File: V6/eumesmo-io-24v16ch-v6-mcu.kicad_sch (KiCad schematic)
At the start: 21 parts, among them Q3 UMH3N, SW1 RESET, U3 TPS3820-33, U4 CH340K, U5 ESP32-WROOM-32UE-N16

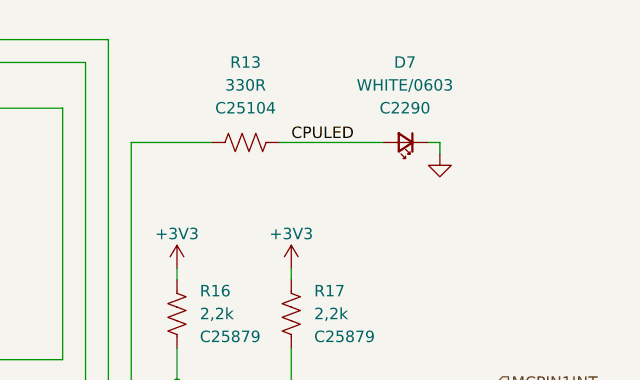
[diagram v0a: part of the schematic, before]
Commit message: Replaced white leds for emerald.
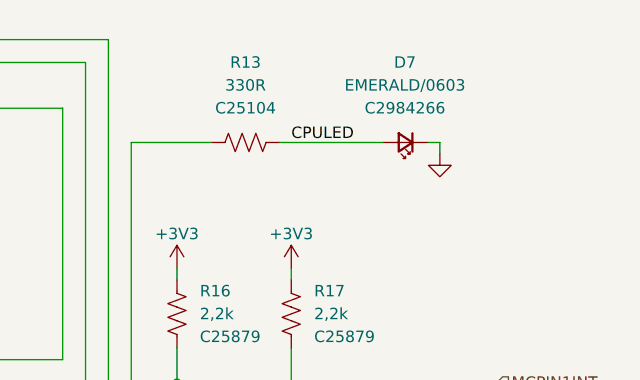
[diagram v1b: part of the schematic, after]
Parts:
- D7: value WHITE/0603 -> EMERALD/0603; LCSC Part # C2290 -> C2984266; Mfr Hubei KENTO Elec -> Everlight Elec; Mfr PN KT-0603W -> 19-213/GHC-XS1T1N/5T; Vendor PN C2290 -> C2984266
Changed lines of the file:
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@@
 			)
 		)
-		(property "Value" "WHITE/0603"
+		(property "Value" "EMERALD/0603"
 			(at 257.7465 35.56 0)
 			(show_name no)
@@
 			)
 		)
-		(property "Mfr" "Hubei KENTO Elec"
+		(property "Mfr" "Everlight Elec"
 			(at 257.81 41.91 0)
 			(hide yes)
@@
 			)
 		)
-		(property "Mfr PN" "KT-0603W"
+		(property "Mfr PN" "19-213/GHC-XS1T1N/5T"
 			(at 257.81 41.91 0)
 			(hide yes)
@@
 			)
 		)
-		(property "Vendor PN" "C2290"
+		(property "Vendor PN" "C2984266"
 			(at 257.81 41.91 0)
 			(hide yes)
@@
 			)
 		)
-		(property "LCSC Part #" "C2290"
+		(property "LCSC Part #" "C2984266"
 			(at 257.7465 38.1 0)
 			(show_name no)

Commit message: Remove jumpers from BOM.
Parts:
- D7: FT Rotation Offset 0 -> 180
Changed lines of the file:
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@@
 			)
 		)
-		(property "FT Rotation Offset" "0"
+		(property "FT Rotation Offset" "180"
 			(at 257.81 41.91 0)
 			(hide yes)

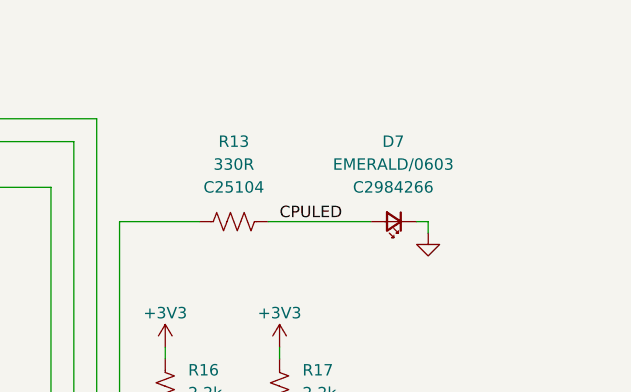
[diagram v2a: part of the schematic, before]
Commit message: LEDs changed to orange
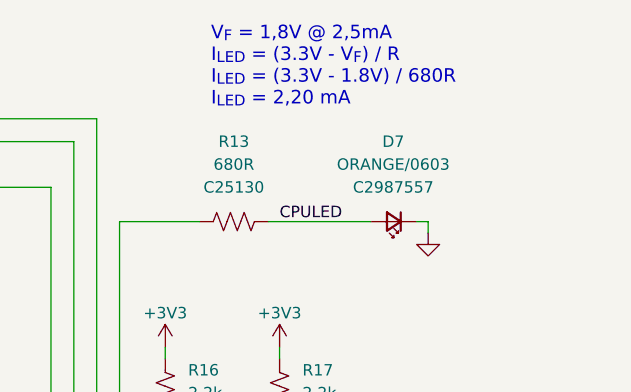
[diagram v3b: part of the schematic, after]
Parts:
- D7: value EMERALD/0603 -> ORANGE/0603; FT Rotation Offset 180 -> 0; LCSC Part # C2984266 -> C2987557; Mfr PN 19-213/GHC-XS1T1N/5T -> 19-217/S2C-AL1M2VY/6T; Vendor PN C2984266 -> C2987557
- R13: value 330R -> 680R; LCSC Part # C25104 -> C25130; Mfr PN 0402WGF3300TCE -> 0402WGF6800TCE; Vendor PN C25104 -> C25130
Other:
- note added: "V_{F} = 1,8V @ 2,5mA I_{LED} = (3.3V - V_{F}) / R I_{LED} = (3.3V - 1.8V) / 680R I_{LED} = 2,20 mA"
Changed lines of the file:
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@@
 		)
 	)
+	(text "V_{F} = 1,8V @ 2,5mA\nI_{LED} = (3.3V - V_{F}) / R\nI_{LED} = (3.3V - 1.8V) / 680R\nI_{LED} = 2,20 mA"
+		(exclude_from_sim no)
+		(at 237.49 29.21 0)
+		(effects
+			(font
+				(size 1.5 1.5)
+			)
+			(justify left bottom)
+		)
+	)
 	(text_box "ESP32 GPIO ASSIGNMENT\n\nPIN	PORT	FUNCTION		COMPONENT\n\n25	GPIO0	AUTO FLASH MODE	0\n35	GPIO1	SERIAL TX		3200\n24	GPIO2	-				0\n34	GPIO3	SERIAL RX		3232\n26	GPIO4	-				0\n29	GPIO5	-				0\n17	GPIO9	-				0\n18	GPIO10	-				0\n14	GPIO12	ETH POWER		5536\n16	GPIO13	MCP23017 INT1	10240\n13	GPIO14	MCP23017 INT2	10241\n23	GPIO15	-				0\n27	GPIO16	DS18X20			1312\n28	GPIO17	ETH CLK			0\n30	GPIO18	ETH MDIO		5600\n31	GPIO19	ETH TXD0		0\n-	GPIO20	-				0\n33	GPIO21	ETH TXEN		0\n36	GPIO22	ETH TXD1		0\n37	GPIO23	ETH MDC			5568\n-	GPIO24	-				0\n10	GPIO25	ETH RXD0		0\n11	GPIO26	ETH RXD1		0\n12	GPIO27	ETH RX			0\n20	GPIO6	-				0\n21	GPIO7	-				0\n22	GPIO8	-				0\n19	GPIO11	-				0\n8	GPIO32	I2C SCL			608\n9	GPIO33	I2C SDA			640\n6	GPIO34	-				0\n7	GPIO35	-				0\n4	GPIO36	-				0\n-	GPIO37	-				0\n-	GPIO38	-				0\n5	GPIO39	-				0"
 		(exclude_from_sim no)
@@
 			)
 		)
-		(property "Value" "EMERALD/0603"
+		(property "Value" "ORANGE/0603"
 			(at 257.7465 35.56 0)
 			(show_name no)
@@
 			)
 		)
-		(property "Mfr PN" "19-213/GHC-XS1T1N/5T"
+		(property "Mfr PN" "19-217/S2C-AL1M2VY/6T"
 			(at 257.81 41.91 0)
 			(hide yes)
@@
 			)
 		)
-		(property "Vendor PN" "C2984266"
+		(property "Vendor PN" "C2987557"
 			(at 257.81 41.91 0)
 			(hide yes)
@@
 			)
 		)
-		(property "LCSC Part #" "C2984266"
+		(property "LCSC Part #" "C2987557"
 			(at 257.7465 38.1 0)
 			(show_name no)
@@
 			)
 		)
-		(property "FT Rotation Offset" "180"
+		(property "FT Rotation Offset" "0"
 			(at 257.81 41.91 0)
 			(hide yes)
@@
 			)
 		)
-		(property "Value" "330R"
+		(property "Value" "680R"
 			(at 240.03 35.56 90)
 			(show_name no)
@@
 			)
 		)
-		(property "Mfr PN" "0402WGF3300TCE"
+		(property "Mfr PN" "0402WGF6800TCE"
 			(at 240.03 41.91 0)
 			(hide yes)
@@
 			)
 		)
-		(property "Vendor PN" "C25104"
+		(property "Vendor PN" "C25130"
 			(at 240.03 41.91 0)
 			(hide yes)
@@
 			)
 		)
-		(property "LCSC Part #" "C25104"
+		(property "LCSC Part #" "C25130"
 			(at 240.03 38.1 90)
 			(show_name no)

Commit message: Adjusted component rotation and offset information for JLCPCB.
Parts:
- U5: FT Position Offset (none) -> 0,-0.65
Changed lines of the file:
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@@
 			)
 		)
+		(property "FT Position Offset" ""
+			(at 257.81 41.91 0)
+			(hide yes)
+			(show_name no)
+			(do_not_autoplace no)
+			(effects
+				(font
+					(size 1.27 1.27)
+				)
+			)
+		)
 		(pin "1"
 		)
@@
 			)
 		)
+		(property "FT Position Offset" ""
+			(at 39.37 67.31 0)
+			(hide yes)
+			(show_name no)
+			(do_not_autoplace no)
+			(effects
+				(font
+					(size 1.27 1.27)
+				)
+			)
+		)
 		(pin "1"
 		)
@@
 			)
 		)
+		(property "FT Position Offset" ""
+			(at 215.9 93.98 90)
+			(hide yes)
+			(show_name no)
+			(do_not_autoplace no)
+			(effects
+				(font
+					(size 1.27 1.27)
+				)
+			)
+		)
 		(pin "2"
 		)
@@
 			)
 		)
-		(property "Package" ""
+		(property "Case" "0805/2012"
 			(at 160.02 53.34 0)
 			(hide yes)
@@
 			)
 		)
-		(property "Case" "0805/2012"
+		(property "FT Rotation Offset" "0"
 			(at 160.02 53.34 0)
 			(hide yes)
@@
 			)
 		)
-		(property "FT Rotation Offset" "0"
+		(property "FT Position Offset" ""
 			(at 160.02 53.34 0)
 			(hide yes)
@@
 			)
 		)
-		(property "Package" ""
+		(property "Case" "0402/1005"
 			(at 123.19 55.88 0)
 			(hide yes)
@@
 			)
 		)
-		(property "Case" "0402/1005"
+		(property "FT Rotation Offset" "0"
 			(at 123.19 55.88 0)
 			(hide yes)
@@
 			)
 		)
-		(property "FT Rotation Offset" "0"
+		(property "FT Position Offset" ""
 			(at 123.19 55.88 0)
 			(hide yes)
@@
 			)
 		)
-		(property "Package" ""
+		(property "Case" "0402/1005"
 			(at 209.55 58.42 0)
 			(hide yes)
@@
 			)
 		)
-		(property "Case" "0402/1005"
+		(property "FT Rotation Offset" "0"
 			(at 209.55 58.42 0)
 			(hide yes)
@@
 			)
 		)
-		(property "FT Rotation Offset" "0"
+		(property "FT Position Offset" ""
 			(at 209.55 58.42 0)
 			(hide yes)
@@
 			)
 		)
+		(property "FT Position Offset" ""
+			(at 182.88 53.34 0)
+			(hide yes)
+			(show_name no)
+			(do_not_autoplace no)
+			(effects
+				(font
+					(size 1.27 1.27)
+				)
+			)
+		)
 		(pin "1"
 		)
@@
 			)
 		)
+		(property "FT Position Offset" ""
+			(at 48.26 67.31 0)
+			(hide yes)
+			(show_name no)
+			(do_not_autoplace no)
+			(effects
+				(font
+					(size 1.27 1.27)
+				)
+			)
+		)
 		(pin "1"
 		)
@@
 			)
 		)
+		(property "FT Position Offset" ""
+			(at 106.68 59.69 0)
+			(hide yes)
+			(show_name no)
+			(do_not_autoplace no)
+			(effects
+				(font
+					(size 1.27 1.27)
+				)
+			)
+		)
 		(pin "1"
 		)
@@
 			)
 		)
+		(property "FT Position Offset" ""
+			(at 106.68 80.01 0)
+			(hide yes)
+			(show_name no)
+			(do_not_autoplace no)
+			(effects
+				(font
+					(size 1.27 1.27)
+				)
+			)
+		)
 		(pin "1"
 		)
@@
 			)
 		)
+		(property "FT Position Offset" ""
+			(at 260.35 109.22 0)
+			(hide yes)
+			(show_name no)
+			(do_not_autoplace no)
+			(effects
+				(font
+					(size 1.27 1.27)
+				)
+			)
+		)
 		(pin "1"
 		)
@@
 			)
 		)
+		(property "FT Position Offset" ""
+			(at 123.19 97.79 90)
+			(hide yes)
+			(show_name no)
+			(do_not_autoplace no)
+			(effects
+				(font
+					(size 1.27 1.27)
+				)
+			)
+		)
 		(pin "1"
 		)
@@
 			)
 		)
-		(property "Package" ""
+		(property "Case" "0805/2012"
 			(at 21.59 48.26 0)
 			(hide yes)
@@
 			)
 		)
-		(property "Case" "0805/2012"
+		(property "FT Rotation Offset" "0"
 			(at 21.59 48.26 0)
 			(hide yes)
@@
 			)
 		)
-		(property "FT Rotation Offset" "0"
+		(property "FT Position Offset" ""
 			(at 21.59 48.26 0)
 			(hide yes)
@@
 			)
 		)
-		(property "Package" ""
+		(property "Case" "0402/1005"
 			(at 257.81 87.63 0)
 			(hide yes)
@@
 			)
 		)
-		(property "Case" "0402/1005"
+		(property "FT Rotation Offset" "0"
 			(at 257.81 87.63 0)
 			(hide yes)
@@
 			)
 		)
-		(property "FT Rotation Offset" "0"
+		(property "FT Position Offset" ""
 			(at 257.81 87.63 0)
 			(hide yes)
@@
 			)
 		)
+		(property "FT Position Offset" ""
+			(at 246.38 109.22 0)
+			(hide yes)
+			(show_name no)
+			(do_not_autoplace no)
+			(effects
+				(font
+					(size 1.27 1.27)
+				)
+			)
+		)
 		(pin "1"
 		)
@@
 			)
 		)
+		(property "FT Position Offset" "0,-0.65"
+			(at 179.07 96.52 0)
+			(hide yes)
+			(show_name no)
+			(do_not_autoplace no)
+			(effects
+				(font
+					(size 1.27 1.27)
+				)
+			)
+		)
 		(pin "1"
 		)
@@
 			)
 		)
+		(property "FT Position Offset" ""
+			(at 245.11 60.96 0)
+			(hide yes)
+			(show_name no)
+			(do_not_autoplace no)
+			(effects
+				(font
+					(size 1.27 1.27)
+				)
+			)
+		)
 		(pin "1"
 		)
@@
 			)
 		)
+		(property "FT Position Offset" ""
+			(at 232.41 60.96 0)
+			(hide yes)
+			(show_name no)
+			(do_not_autoplace no)
+			(effects
+				(font
+					(size 1.27 1.27)
+				)
+			)
+		)
 		(pin "1"
 		)
@@
 			)
 		)
+		(property "FT Position Offset" ""
+			(at 240.03 41.91 90)
+			(hide yes)
+			(show_name no)
+			(do_not_autoplace no)
+			(effects
+				(font
+					(size 1.27 1.27)
+				)
+			)
+		)
 		(pin "1"
 		)
@@
 			)
 		)
+		(property "FT Position Offset" ""
+			(at 143.51 66.04 0)
+			(hide yes)
+			(show_name no)
+			(do_not_autoplace no)
+			(effects
+				(font
+					(size 1.27 1.27)
+				)
+			)
+		)
 		(pin "3"
 		)
@@
 			)
 		)
+		(property "FT Position Offset" ""
+			(at 63.5 72.39 0)
+			(hide yes)
+			(show_name no)
+			(do_not_autoplace no)
+			(effects
+				(font
+					(size 1.27 1.27)
+				)
+			)
+		)
 		(pin "2"
 		)
@@
 			)
 		)
-		(property "Package" ""
+		(property "Case" "0402/1005"
 			(at 43.18 48.26 0)
 			(hide yes)
@@
 			)
 		)
-		(property "Case" "0402/1005"
+		(property "FT Rotation Offset" "0"
 			(at 43.18 48.26 0)
 			(hide yes)
@@
 			)
 		)
-		(property "FT Rotation Offset" "0"
+		(property "FT Position Offset" ""
 			(at 43.18 48.26 0)
 			(hide yes)

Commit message: Replaced Wago connectors for other brand, no stock.
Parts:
- R13: LCSC Part # C25130 -> C137948; Mfr Uniroyal -> YAGEO; Mfr PN 0402WGF6800TCE -> RC0402FR-07680RL; Vendor PN C25130 -> C137948
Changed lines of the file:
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@@
 			)
 		)
-		(property "Mfr" "Uniroyal"
+		(property "Mfr" "YAGEO"
 			(at 240.03 41.91 0)
 			(hide yes)
@@
 			)
 		)
-		(property "Mfr PN" "0402WGF6800TCE"
+		(property "Mfr PN" "RC0402FR-07680RL"
 			(at 240.03 41.91 0)
 			(hide yes)
@@
 			)
 		)
-		(property "Vendor PN" "C25130"
+		(property "Vendor PN" "C137948"
 			(at 240.03 41.91 0)
 			(hide yes)
@@
 			)
 		)
-		(property "LCSC Part #" "C25130"
+		(property "LCSC Part #" "C137948"
 			(at 240.03 38.1 90)
 			(show_name no)
